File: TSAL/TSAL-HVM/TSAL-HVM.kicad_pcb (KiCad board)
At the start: 2 copper layers, 80.9 x 57.8 mm, 48 parts, among them J1 HV+, J2 HV-, J3 Conn_01x03_Male, J4 VHI, K1 TE_PCH-1xxx2M, Q1 2N7002, Q2 2N7002, Q3 2N7002, U1 SPAN02A-12, U2 LM311

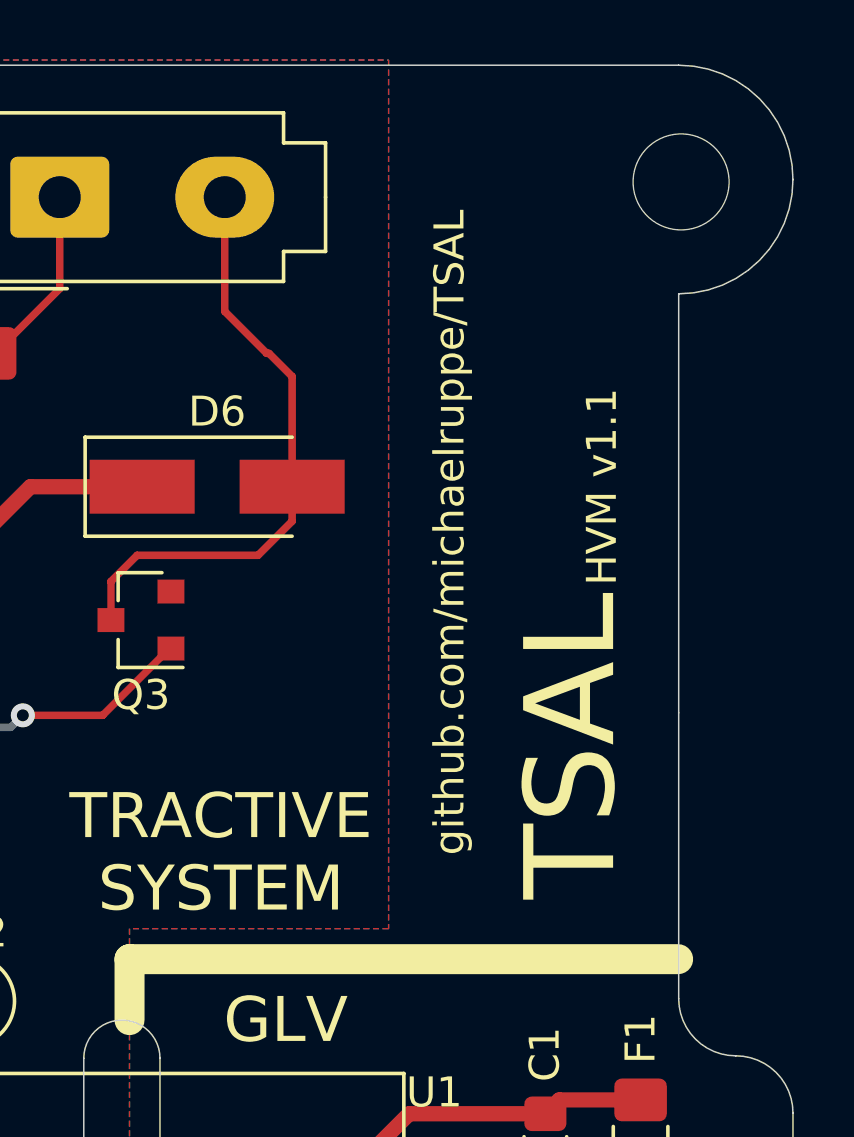
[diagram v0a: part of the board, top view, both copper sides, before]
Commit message: Update schematic title blocks, READMEs, Schematic.pdfs
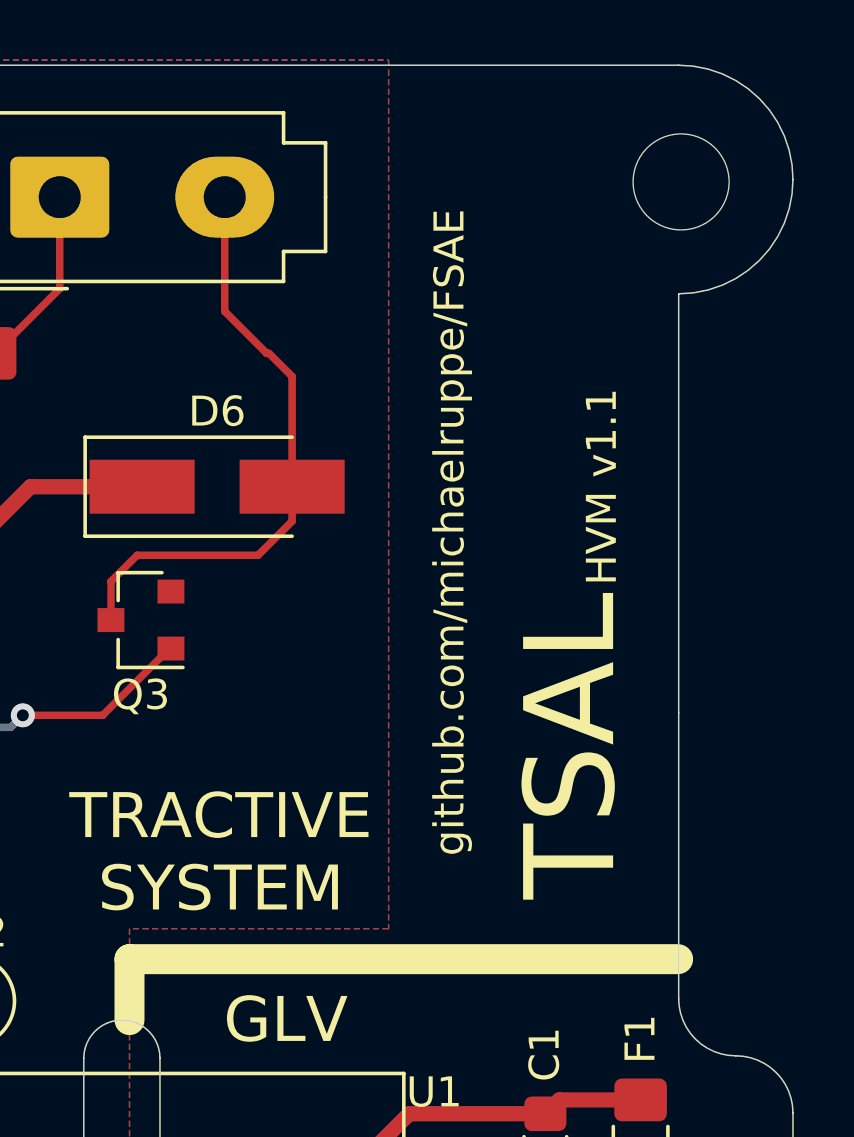
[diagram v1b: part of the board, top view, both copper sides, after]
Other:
- board text added: "github.com/michaelruppe/FSAE"
- board text removed: "github.com/michaelruppe/TSAL"
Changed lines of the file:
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@@
     (effects (font (size 2 2) (thickness 0.3)))
   )
-  (gr_text github.com/michaelruppe/TSAL (at 117.602 56.134 90) (layer F.SilkS)
+  (gr_text github.com/michaelruppe/FSAE (at 117.602 56.134 90) (layer F.SilkS)
     (effects (font (size 1 1) (thickness 0.15)))
   )

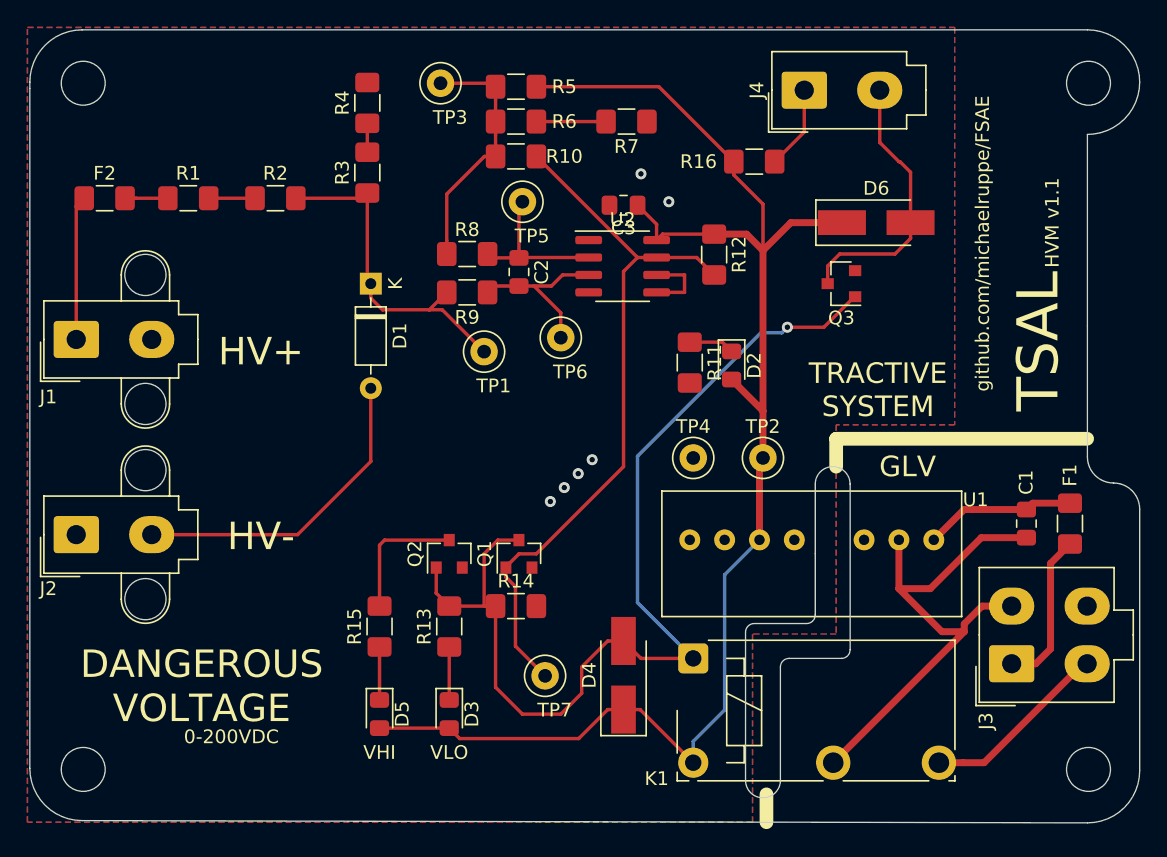
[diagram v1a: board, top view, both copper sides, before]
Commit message: Update TSAL-HVMv1.1 with lessons learned from assembling v1
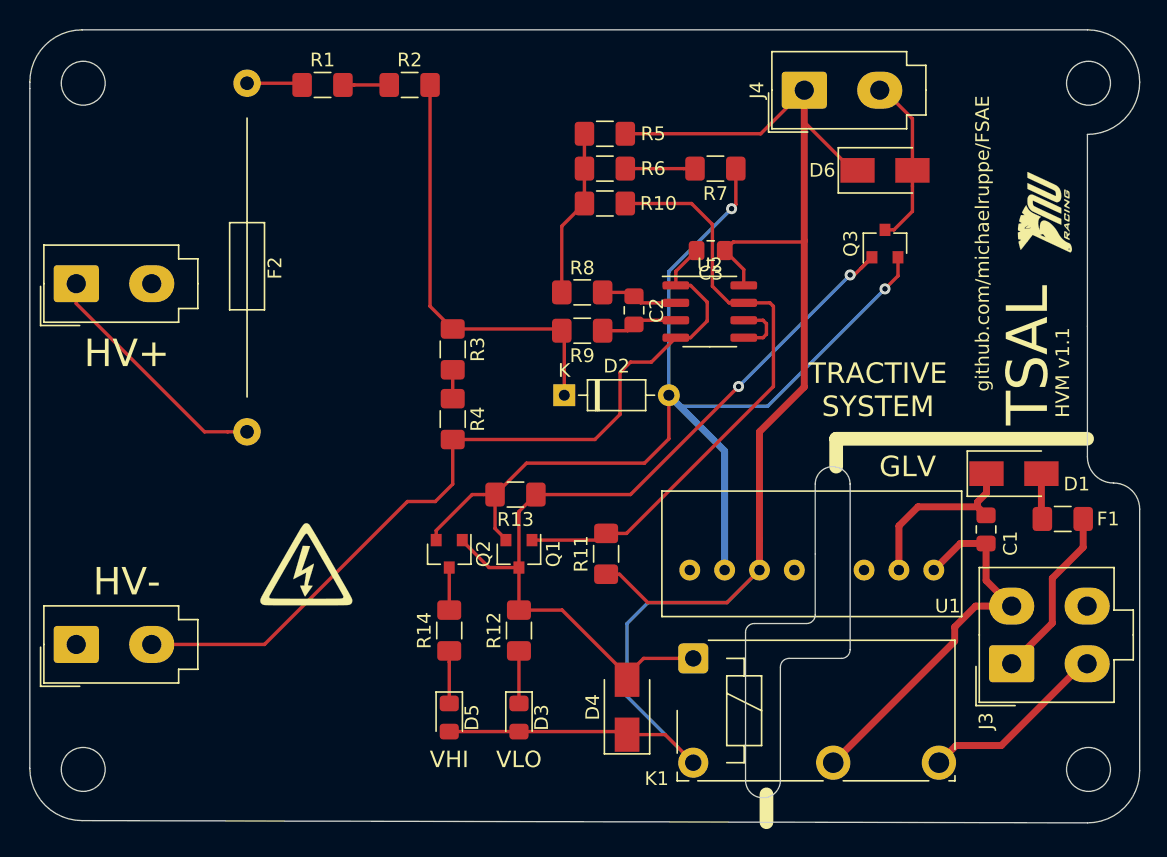
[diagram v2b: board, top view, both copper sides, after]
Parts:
- removed R15: 2k2, Resistor_SMD:R_1206_3216Metric_Pad1.42x1.75mm_HandSolder
- removed R16: PRV, Resistor_SMD:R_1206_3216Metric_Pad1.42x1.75mm_HandSolder
- removed TP1, TP3, TP5, TP6, TP7: TestPoint, TestPoint:TestPoint_Loop_D1.80mm_Drill1.0mm_Beaded
- removed TP2: +12, TestPoint:TestPoint_Loop_D1.80mm_Drill1.0mm_Beaded
- removed TP4: GND, TestPoint:TestPoint_Loop_D1.80mm_Drill1.0mm_Beaded
- added G***: LOGO, TSAL-HVM:logo, F.Cu at (122.2, 53.8)
- added G***: LOGO, TSAL-HVM:electric-shock-symbol, F.Cu at (68.3, 79.5)
- D1: value 12V -> D; footprint Diode_THT:D_DO-35_SOD27_P7.62mm_Horizontal -> Diode_SMD:D_SMA
- D2: value PWR -> 12V; footprint LED_SMD:LED_0805_2012Metric_Pad1.15x1.40mm_HandSolder -> Diode_THT:D_DO-35_SOD27_P7.62mm_Horizontal
- D4, D6: footprint Diode_SMD:D_SMA_Handsoldering -> Diode_SMD:D_SMA
- F2: footprint Fuse:Fuse_1206_3216Metric_Pad1.42x1.75mm_HandSolder -> TSAL-HVM:BELFUSE-5HF
- J1, J2: footprint Connector_Molex:Molex_Mini-Fit_Jr_5566-02A2_2x01_P4.20mm_Vertical -> Connector_Molex:Molex_Mini-Fit_Jr_5566-02A_2x01_P4.20mm_Vertical
- R11, R13: value 2k2 -> 24k
- R12, R14: value 24k -> 2k2
- moved D1 48.9 mm to (119.9, 72.9), turned to 0 degrees
- moved R12 30.9 mm to (83.8, 84.3), turned to 90 degrees
- moved R4 23.9 mm to (79.0, 68.9), turned to 270 degrees
- moved R11 15.2 mm to (90.2, 78.7), turned to 90 degrees
- moved R3 14.3 mm to (79.0, 63.8), turned to 270 degrees
- moved R2 12.8 mm to (75.9, 44.6)
- moved R1 12.8 mm to (69.5, 44.6)
- moved D2 12.4 mm to (87.1, 67.2), turned to 0 degrees
- moved F2 11.8 mm to (64.0, 58.4), turned to 90 degrees
- moved R13 10.8 mm to (83.6, 74.4), turned to 180 degrees
- moved R9 8.84 mm to (88.4, 62.5)
- moved C2 8.84 mm to (92.2, 61.0)
- moved R8 8.84 mm to (88.4, 59.7)
- moved J2 8.00 mm to (51.6, 85.3)
- moved R7 7.33 mm to (98.1, 50.7)
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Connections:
- C1 pad 1: Net-(C1-Pad1) -> -Vin
- C1 pad 2: -Vin -> Net-(C1-Pad2)
- D1 pad 1: Net-(D1-Pad1) -> Net-(C1-Pad2)
- D1 pad 2: GND -> Net-(D1-Pad2)
- D2 pad 2: +12V -> GND
- F1 pad 2: Net-(C1-Pad1) -> Net-(D1-Pad2)
- J4 pad 1: Net-(J4-Pad1) -> +12V
- R11 pad 1: Net-(D2-Pad1) -> +12V
- R11 pad 2: GND -> Net-(Q1-Pad1)
- R12 pad 1: +12V -> Net-(D3-Pad1)
- R12 pad 2: Net-(Q1-Pad1) -> Net-(D4-Pad2)
- R13 pad 1: Net-(D3-Pad1) -> Net-(D4-Pad2)
- R13 pad 2: Net-(D4-Pad2) -> GND
- R14 pad 1: Net-(D4-Pad2) -> Net-(D5-Pad1)
- R14 pad 2: GND -> Net-(Q2-Pad3)
- R2 pad 2: Net-(D1-Pad1) -> Net-(D2-Pad1)
- R3 pad 1: Net-(D1-Pad1) -> Net-(D2-Pad1)
- R9 pad 2: Net-(D1-Pad1) -> Net-(D2-Pad1)
- U1 pad 1: Net-(C1-Pad1) -> -Vin
- U1 pad 2: -Vin -> Net-(C1-Pad2)
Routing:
- net GND: track 23.5 -> 143.8 mm, vias 6 -> 2
- net Net-(D2-Pad1): track 3.33 -> 31.2 mm
- net Net-(D1-Pad1): track 24.8 -> 0.00 mm
- net Net-(D4-Pad2): track 76.2 -> 62.2 mm, vias 1 -> 2
- net Net-(C1-Pad2): track 0.00 -> 13.1 mm
- net +12V: track 110.5 -> 122.7 mm
- net Net-(C1-Pad1): track 11.0 -> 0.00 mm
- net -Vin: track 38.5 -> 28.7 mm
- net Net-(Q1-Pad1): track 52.9 -> 44.7 mm
- net Net-(D6-Pad2): track 19.9 -> 12.5 mm
- net /+HV: track 10.5 -> 17.8 mm
- net Net-(C2-Pad2): track 12.5 -> 5.65 mm
- net Net-(Q2-Pad3): track 9.68 -> 3.10 mm
- net Net-(J4-Pad1): track 6.10 -> 0.00 mm
- net Net-(C2-Pad1): track 11.7 -> 5.65 mm
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- removed copper zone on B.Cu, net GND
- removed copper zone on F.Cu, net GND
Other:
- board text removed: "0-200VDC"
- board text removed: "DANGEROUS VOLTAGE"
